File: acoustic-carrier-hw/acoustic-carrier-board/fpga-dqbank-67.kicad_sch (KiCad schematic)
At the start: 8 parts, among them IC1 ECP5-BGA256

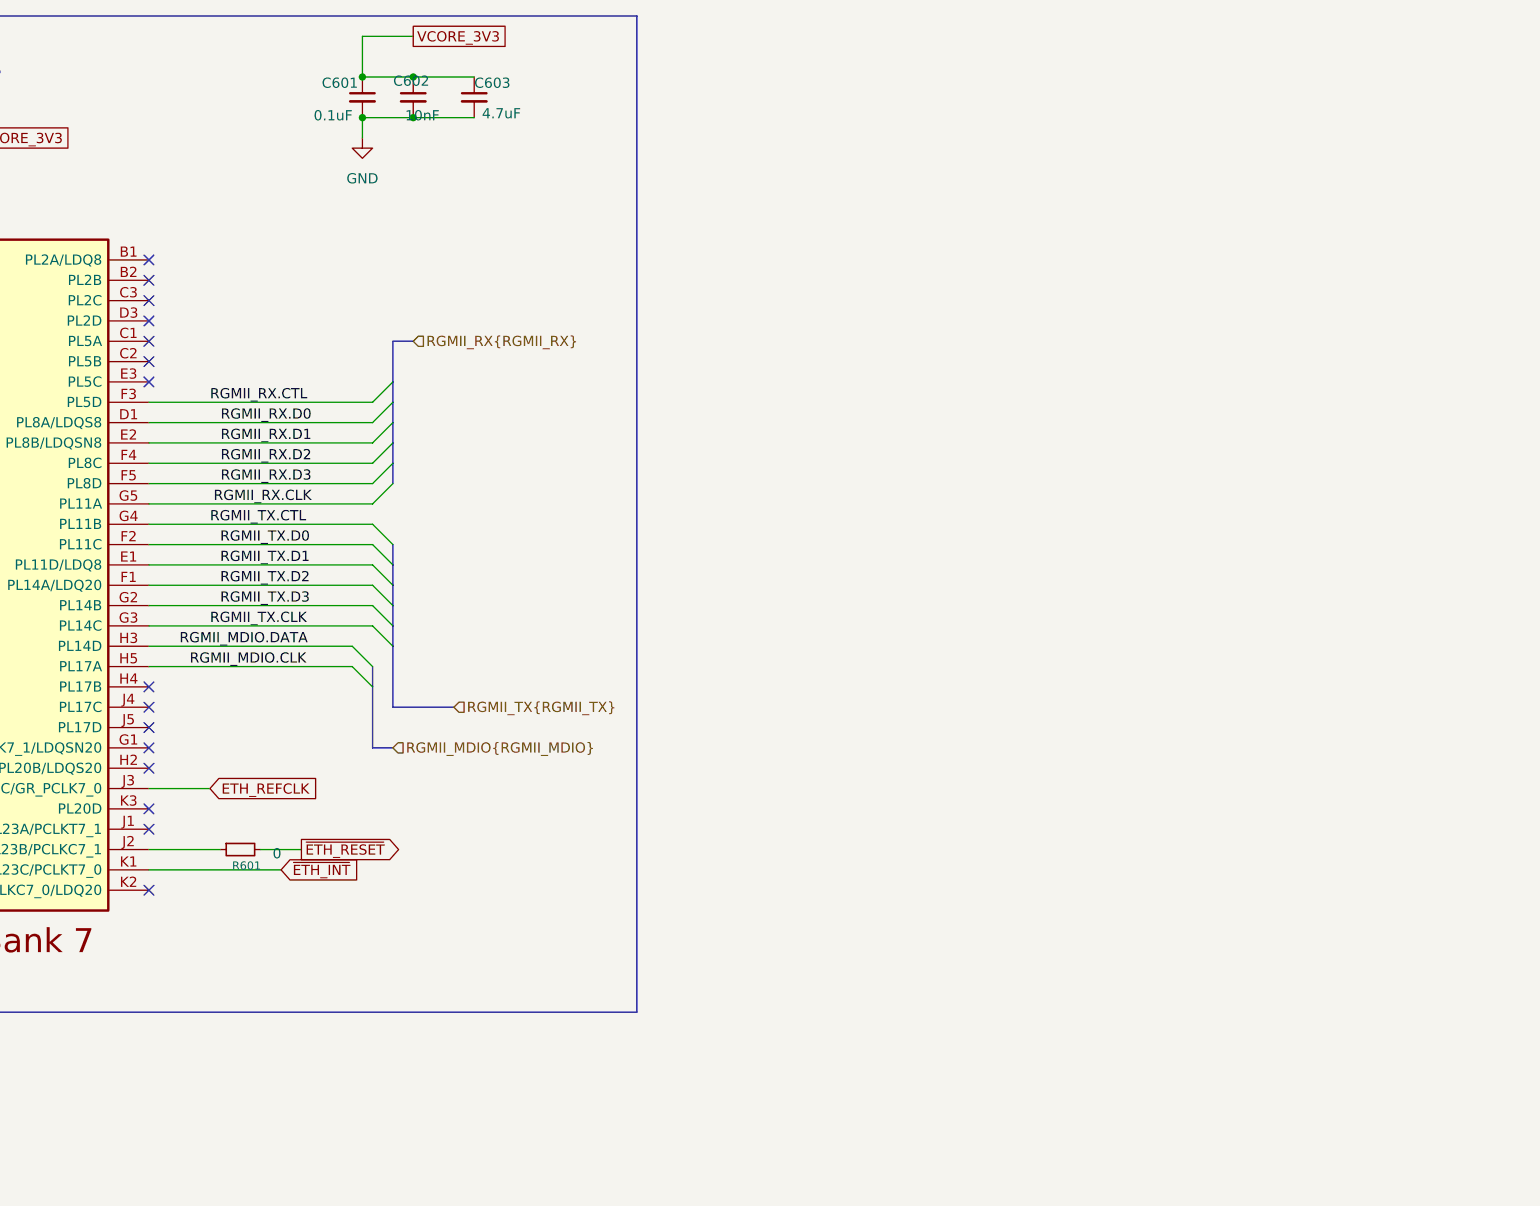
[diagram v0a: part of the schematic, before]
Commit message: [carrier] Routing out RGMII interface
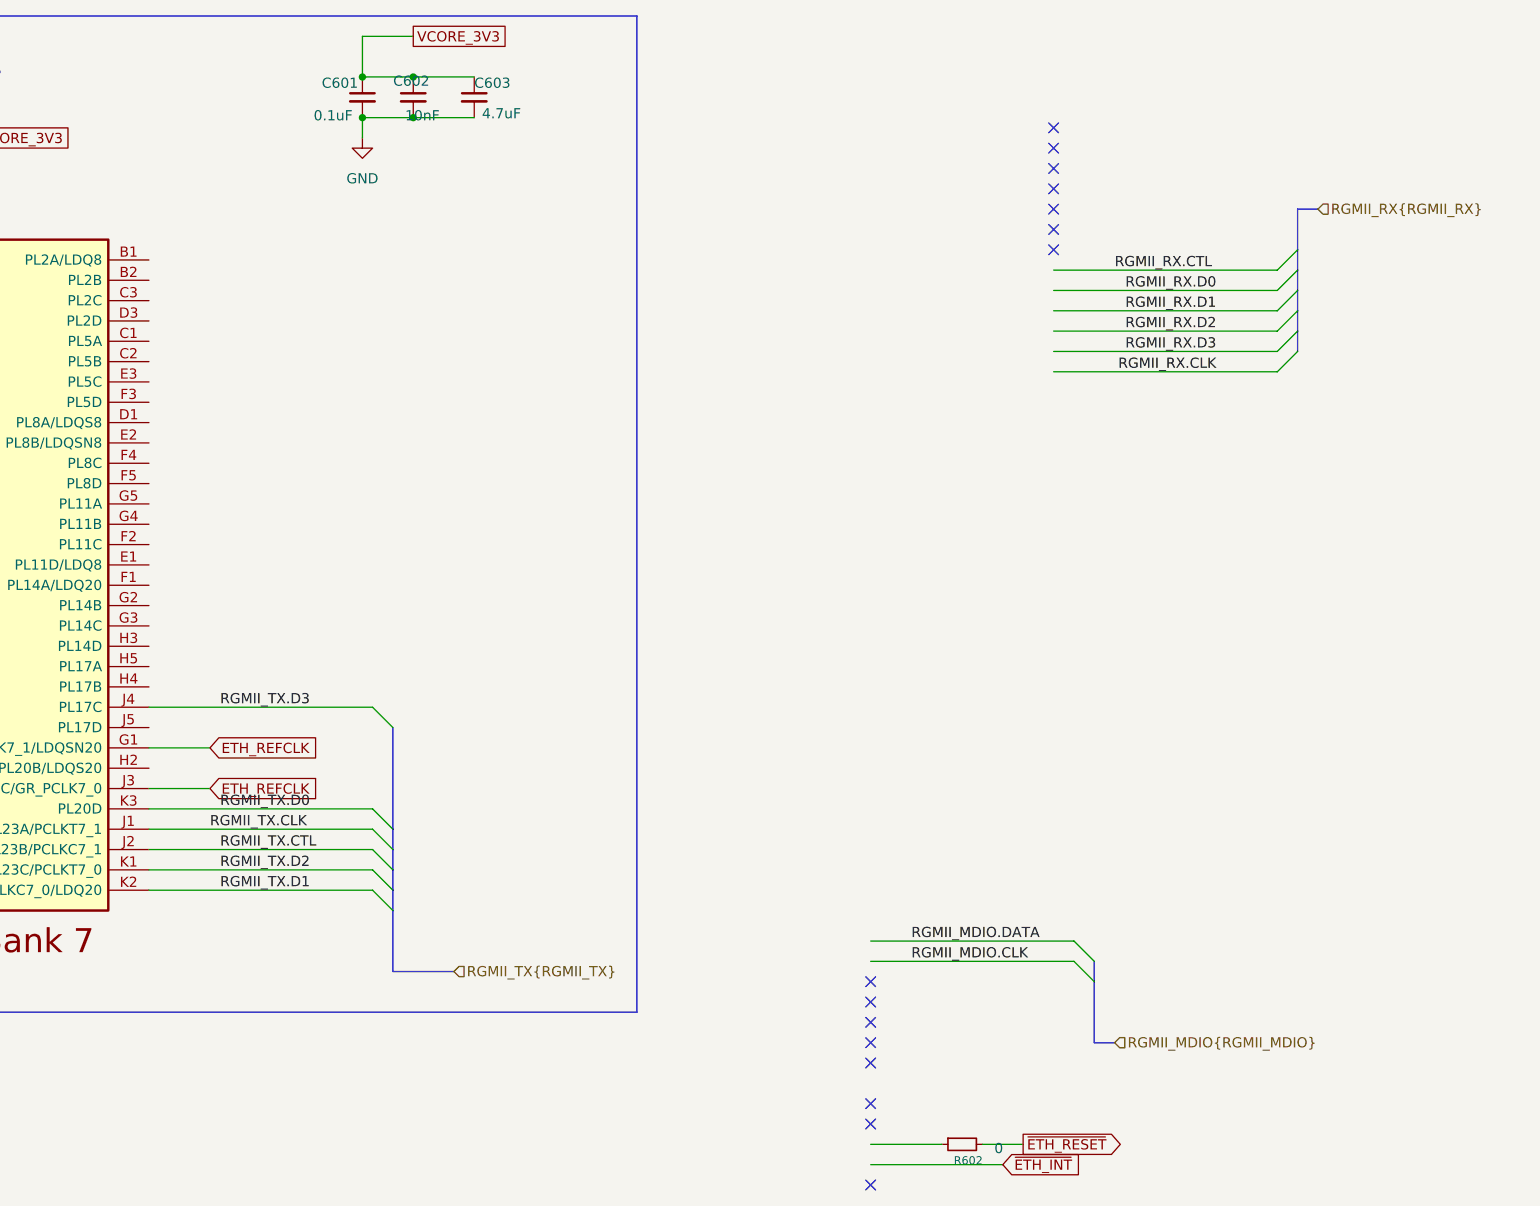
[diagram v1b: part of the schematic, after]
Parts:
- removed R601: 0, Resistor_SMD:R_0603_1608Metric, symbol Device:R_Small
- added R602: 0, Resistor_SMD:R_0603_1608Metric, symbol Device:R_Small
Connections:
- net ETH_REFCLK: now also IC1.G1 (PL20A/GR_PCLK7_1/LDQSN20)
- net RGMII_MDIO.CLK: no longer IC1.H5 (PL17A)
- net RGMII_MDIO.DATA: no longer IC1.H3 (PL14D)
- net RGMII_RX.CLK: no longer IC1.G5 (PL11A)
- net RGMII_RX.CTL: no longer IC1.F3 (PL5D)
- net RGMII_RX.D0: no longer IC1.D1 (PL8A/LDQS8)
- net RGMII_RX.D1: no longer IC1.E2 (PL8B/LDQSN8)
- net RGMII_RX.D2: no longer IC1.F4 (PL8C)
- net RGMII_RX.D3: no longer IC1.F5 (PL8D)
- net RGMII_TX.CLK: now also IC1.J1 (PL23A/PCLKT7_1); no longer IC1.G3 (PL14C)
- net RGMII_TX.CTL: now also IC1.J2 (PL23B/PCLKC7_1); no longer IC1.G4 (PL11B)
- net RGMII_TX.D0: now also IC1.K3 (PL20D); no longer IC1.F2 (PL11C)
- net RGMII_TX.D1: now also IC1.K2 (PL23D/PCLKC7_0/LDQ20); no longer IC1.E1 (PL11D/LDQ8)
- net RGMII_TX.D2: now also IC1.K1 (PL23C/PCLKT7_0); no longer IC1.F1 (PL14A/LDQ20)
- net RGMII_TX.D3: now also IC1.J4 (PL17C); no longer IC1.G2 (PL14B)
- net ~{ETH_INT}: no longer IC1.K1 (PL23C/PCLKT7_0)
- net ~{ETH_RESET}: now also R602.2

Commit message: Did big ig parts of routing (next) make sure to re-add pull-ups/downs accordingly
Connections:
- net ADC.CLK: now also IC1.T2 (PL38D); no longer IC1.P6 (PL47C/LLC_GPLL0T_IN)
- net ADC.D0: now also IC1.M6 (PL47A); no longer IC1.P5 (PL47D/LLC_GPLL0C_IN)
- net ADC.D1: now also IC1.P6 (PL47C/LLC_GPLL0T_IN); no longer IC1.N6 (PL47B)
- net ADC.D2: now also IC1.N6 (PL47B); no longer IC1.M6 (PL47A)
- net ADC.D3: now also IC1.R5 (PL44A/LDQS44); no longer IC1.T3 (PL41D)
- net ADC.D4: now also IC1.P5 (PL47D/LLC_GPLL0C_IN); no longer IC1.R4 (PL41C)
- net ADC.D5: now also IC1.N5 (PL44D); no longer IC1.R3 (PL41B)
- net ADC.D6: now also IC1.T4 (PL44B/LDQSN44); no longer IC1.P4 (PL41A)
- net ADC.D7: now also IC1.P4 (PL41A); no longer IC1.N5 (PL44D)
- net ADC.D8: now also IC1.R4 (PL41C); no longer IC1.M5 (PL44C)
- net ADC.D9: now also IC1.T3 (PL41D); no longer IC1.T4 (PL44B/LDQSN44)
- net ADC.OTR: now also IC1.R3 (PL41B); no longer IC1.R5 (PL44A/LDQS44)
- net CON1.B40_EN: no longer IC1.K5 (PL29B)
- net CON1.PWM0: no longer IC1.L1 (PL26A/LDQ32/PCLKT6_1)
- net CON1.PWM1: no longer IC1.L2 (PL26B/PCLKC6_1)
- net CON1.PWM2: no longer IC1.M1 (PL26C/PCLKT6_0)
- net CON1.PWM3: no longer IC1.M2 (PL26D/PCLKC6_0)
- net CON1.S10V_EN: no longer IC1.K4 (PL29A/GR_PCLK6_0)
- net CON1.T_SCL: no longer IC1.L4 (PL29C/PL29C)
- net CON1.T_SDA: no longer IC1.L5 (PL29D)
- net ETH_REFCLK: no longer IC1.J3 (PL20C/GR_PCLK7_0)
- net FPGA_ADC_SW: no longer IC1.T2 (PL38D)
- net RGMII_MDIO.CLK: now also IC1.G2 (PL14B)
- net RGMII_MDIO.DATA: now also IC1.G3 (PL14C)
- net RGMII_RX.CLK: now also IC1.G5 (PL11A)
- net RGMII_RX.CTL: now also IC1.G4 (PL11B)
- net RGMII_RX.D0: now also IC1.H2 (PL20B/LDQS20)
- net RGMII_RX.D1: now also IC1.H3 (PL14D)
- net RGMII_RX.D2: now also IC1.H4 (PL17B)
- net RGMII_RX.D3: now also IC1.H5 (PL17A)
- net ~{ETH_INT}: now also IC1.E1 (PL11D/LDQ8)
- net FPGA_ADC_LED0: no longer names the net of IC1.R2 (PL38C)
- net FPGA_ADC_LED1: no longer names the net of IC1.P3 (PL38B)
- no-connect marks 24 -> 27
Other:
- moved on the sheet: C611, C612, C613

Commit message: [carrier] Redid routing to PMOD SPI-flash ah (next) add second PMOD-connector and third connector meant for PWM signalling to power board
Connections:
- net CON1.B40_EN: now also IC1.K5 (PL29B)
- net CON1.PWM0: now also IC1.L1 (PL26A/LDQ32/PCLKT6_1)
- net CON1.PWM1: now also IC1.L2 (PL26B/PCLKC6_1)
- net CON1.PWM2: now also IC1.M1 (PL26C/PCLKT6_0)
- net CON1.PWM3: now also IC1.M2 (PL26D/PCLKC6_0)
- net CON1.S10V_EN: now also IC1.K4 (PL29A/GR_PCLK6_0)
- net CON1.T_SCL: now also IC1.L4 (PL29C/PL29C)
- net CON1.T_SDA: now also IC1.L5 (PL29D)
- net FPGA_ADC_SW: now also IC1.P3 (PL38B)
- no-connect marks 27 -> 28
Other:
- moved on the sheet: R602

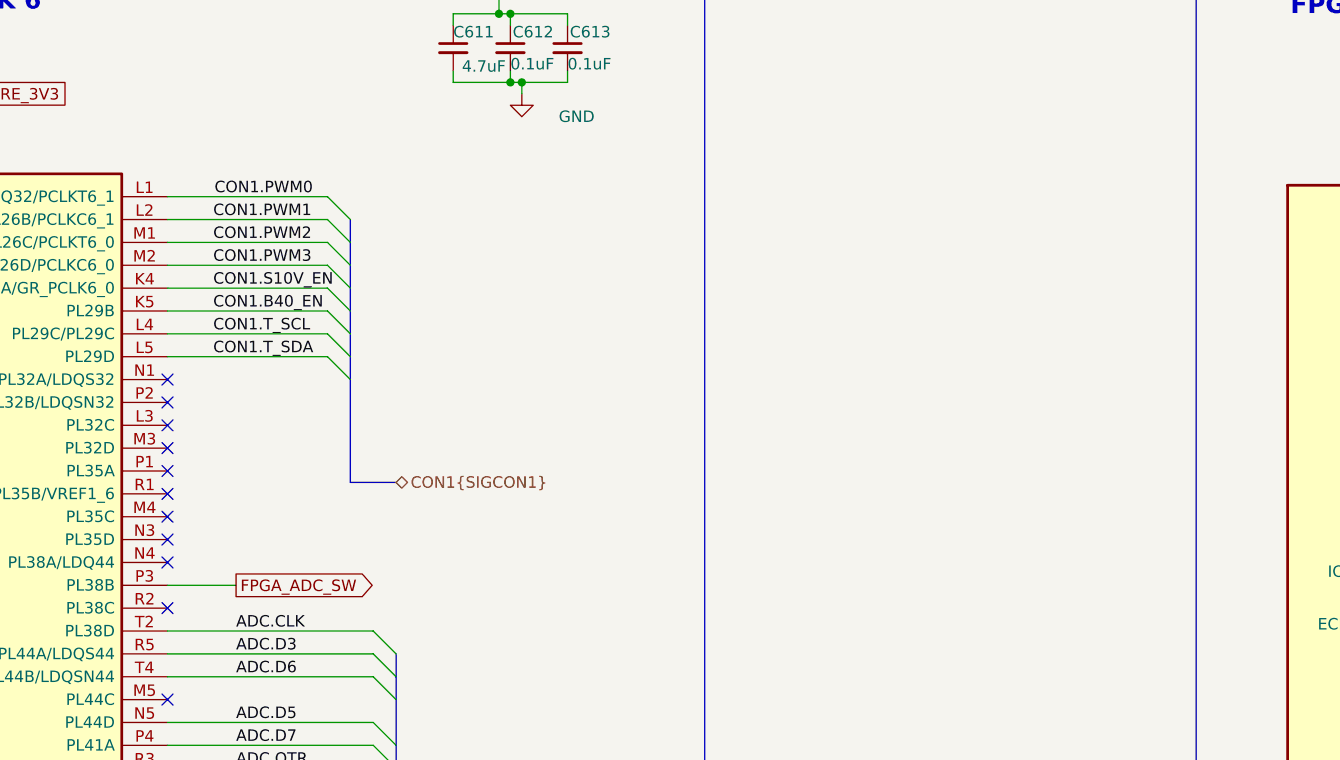
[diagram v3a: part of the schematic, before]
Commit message: [carrier] Routed 6x2 IO connector
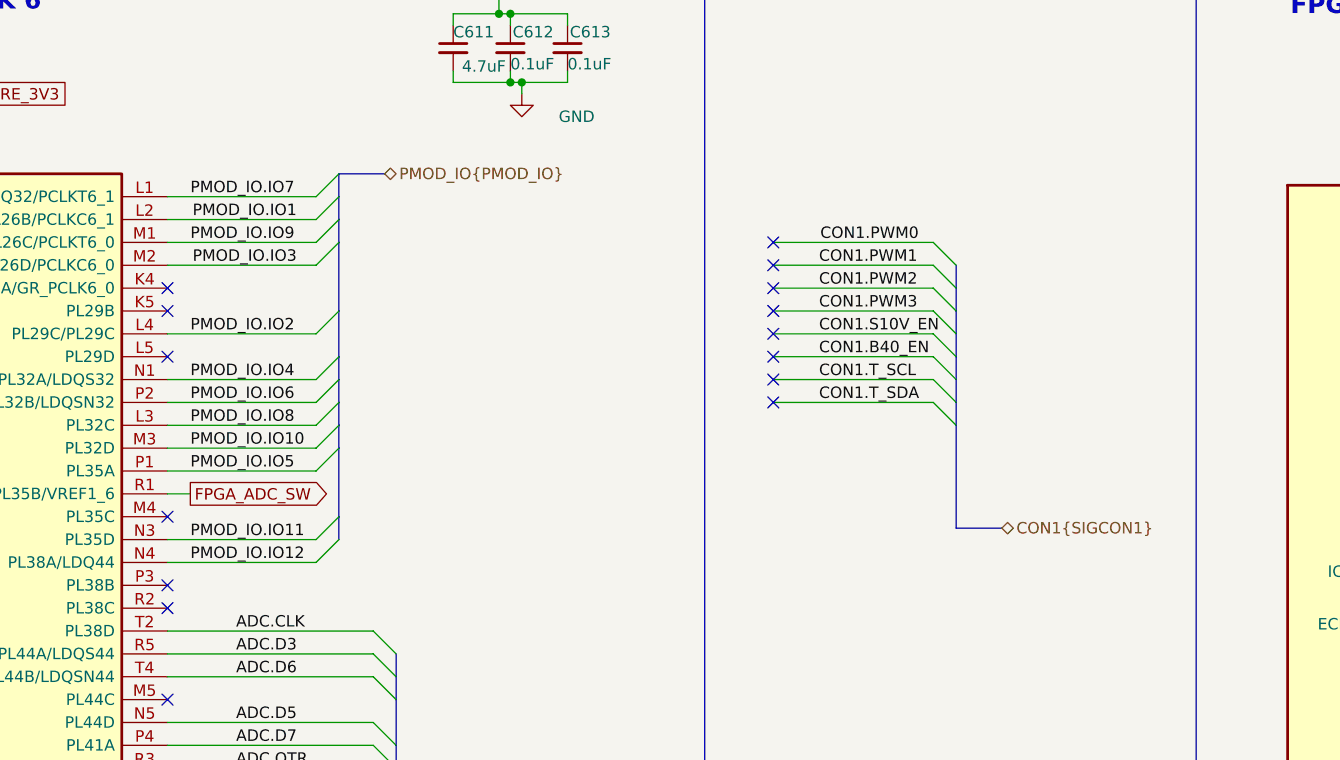
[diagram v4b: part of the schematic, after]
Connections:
- net CON1.B40_EN: no longer IC1.K5 (PL29B)
- net CON1.PWM0: no longer IC1.L1 (PL26A/LDQ32/PCLKT6_1)
- net CON1.PWM1: no longer IC1.L2 (PL26B/PCLKC6_1)
- net CON1.PWM2: no longer IC1.M1 (PL26C/PCLKT6_0)
- net CON1.PWM3: no longer IC1.M2 (PL26D/PCLKC6_0)
- net CON1.S10V_EN: no longer IC1.K4 (PL29A/GR_PCLK6_0)
- net CON1.T_SCL: no longer IC1.L4 (PL29C/PL29C)
- net CON1.T_SDA: no longer IC1.L5 (PL29D)
- net FPGA_ADC_SW: now also IC1.R1 (PL35B/VREF1_6); no longer IC1.P3 (PL38B)
- net PMOD_IO.IO8: now reaches IC1.L3 (PL32C)
- net PMOD_IO.IO10: now reaches IC1.M3 (PL32D)
- net PMOD_IO.IO4: now reaches IC1.N1 (PL32A/LDQS32)
- net PMOD_IO.IO11: now reaches IC1.N3 (PL35D)
- net PMOD_IO.IO12: now reaches IC1.N4 (PL38A/LDQ44)
- net PMOD_IO.IO5: now reaches IC1.P1 (PL35A)
- net PMOD_IO.IO6: now reaches IC1.P2 (PL32B/LDQSN32)
- new net PMOD_IO.IO1: IC1.L2 (PL26B/PCLKC6_1)
- new net PMOD_IO.IO2: IC1.L4 (PL29C/PL29C)
- new net PMOD_IO.IO3: IC1.M2 (PL26D/PCLKC6_0)
- new net PMOD_IO.IO7: IC1.L1 (PL26A/LDQ32/PCLKT6_1)
- new net PMOD_IO.IO9: IC1.M1 (PL26C/PCLKT6_0)
- no-connect marks 28 -> 32

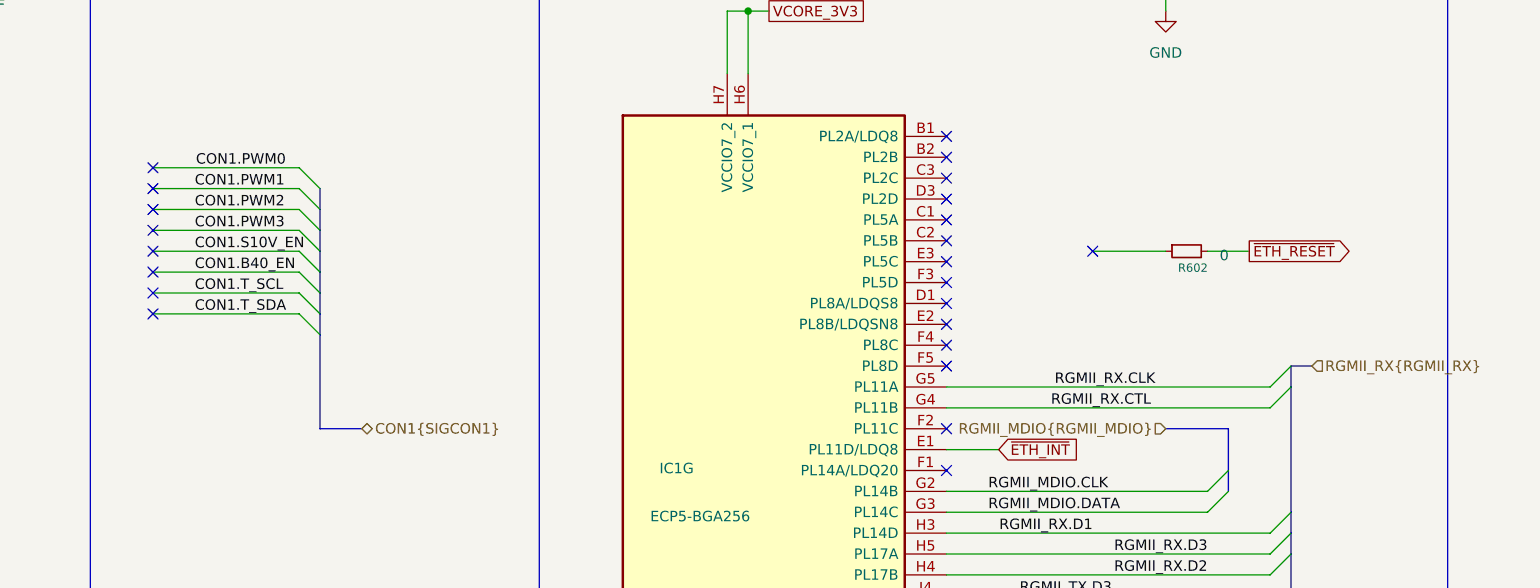
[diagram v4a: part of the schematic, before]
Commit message: [carrier] Routed out signals for board-to-board PTH
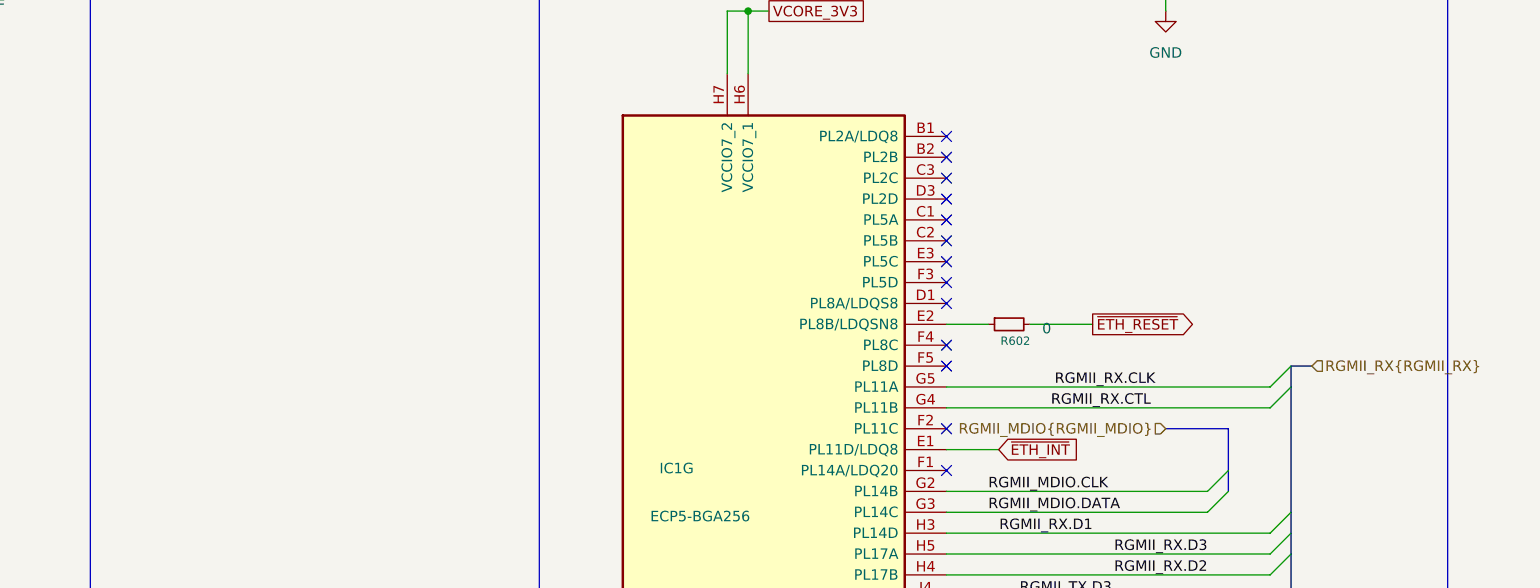
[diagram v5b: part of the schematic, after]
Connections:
- net at R602.1: now also IC1.E2 (PL8B/LDQSN8)
- no-connect marks 32 -> 22
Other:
- moved on the sheet: R602
